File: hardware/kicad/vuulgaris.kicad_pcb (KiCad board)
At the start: 2 copper layers, 284.3 x 125 mm, 69 parts, among them J1 TFPUSH, J10 PJ-603_C41409498, J11 TYPE-C-31-M-12, J2 PJ-376, J3 PJ-376, J4 PJ-376, J5 PJ-376, J7 PJ-603_C41409498, J8 PJ-603_C41409498, J9 PJ-603_C41409498, SW4 CPG151101S03, SW5 CPG151101S03, SW6 CPG151101S03, SW7 CPG151101S03, U1 ES_DAISY_PATCH_SM_REV1, U3 MCP23017-E_SO, U4 MCP23017-E_SO, U5 AMS1117-3.3, U6 AMS1117-3.3, U7 DKM10E-12

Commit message: hardware: place the Daisy for the signals, and fix place.py's mirror flag
MIDI is dropped -- firmware goes on by opening the box -- so the micro-USB no
longer has to reach a wall and the Daisy's placement is unconstrained. It goes in
the dead band between the pot row and the electrodes, x[125.5,193.5] y[42.5,82.5].

Not beside the power stage. That is the intuitive answer and it is backwards:
weighting wire length by how much length actually hurts each signal, sitting on
the power stage scores 11875 against 5611. It does buy the shortest rails, 109mm
against 355mm, and that is worth almost nothing -- they are DC, so widen the
trace and the loss is millivolts. It pays for them with 244mm of extra analog
audio and 651mm of extra CV routed straight over the capacitive electrodes.

The scoring has a real hole worth knowing about: J2-J5 and J7-J10 are placed but
unwired, so netmap.json does not know where audio or CV terminate. The first run
silently returned empty AUDIO and CV columns and ranked the options on SPI and
power alone -- the two classes the argument does not rest on. Destinations are
supplied by hand for now; redo it once the jacks are wired.

Separately, place.py had `Lm` assigned in the pad-orientation loop and read again
in the overlap loop, where it held whatever footprint the earlier loop ended on.
Every box in the overlap and edge checks got the same arbitrary mirror flag. It
invented a 3.18mm RV3/RV4-vs-U1 collision, which is how it was noticed -- RV4's
local y is [-9.14,+4.4] and mirrored reads [-4.4,+9.14], moving its bottom edge
4.74mm. A check that fabricates a collision will hide one just as quietly. Third
mirror bug in this file.
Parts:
- moved U1 89.2 mm to (259.5, 112.5)
- moved J1 12.0 mm to (238.4, 142.1)
- turned J11 to 0 degrees
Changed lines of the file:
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@@
   )
   (footprint "vuulgaris:DAISY_PATCH_SM" (layer "F.Cu")
-    (at 180.0 153.0)
+    (at 259.5 112.5)
     (property "Sheetfile" "vuulgaris.kicad_sch")
     (property "Sheetname" "")
@@
   )
   (footprint "vuulgaris:USB-C_SMD-TYPE-C-31-M-12_1" (layer "B.Cu")
-    (at 379.2 54.0 -90)
+    (at 379.2 54.0)
     (property "Sheetfile" "vuulgaris.kicad_sch")
     (property "Sheetname" "")
     (property "ki_keywords" "USB Connectors")
     (attr smd)
-    (fp_text reference "J11" (at 0 6.474 90) (layer "B.SilkS")
+    (fp_text reference "J11" (at 0 6.474) (layer "B.SilkS")
         (effects (font (size 1 1) (thickness 0.15)) (justify mirror))
     )
-    (fp_text value "TYPE-C-31-M-12" (at 0 -6.474 90) (layer "B.Fab")
+    (fp_text value "TYPE-C-31-M-12" (at 0 -6.474) (layer "B.Fab")
         (effects (font (size 1 1) (thickness 0.15)) (justify mirror))
     )
-    (fp_text user "${REFERENCE}" (at 0 0 90) (layer "B.Fab")
+    (fp_text user "${REFERENCE}" (at 0 0) (layer "B.Fab")
         (effects (font (size 1 1) (thickness 0.15)) (justify mirror))
     )
@@
     (fp_line (start 4.47 2.26) (end 4.47 -5.09)
       (stroke (width 0.05) (type solid)) (layer "B.CrtYd"))
-    (pad "" thru_hole circle (at -2.9 1.21 270) (size 0.6 0.6) (drill 0.6) (layers "*.Cu" "*.Mask"))
-    (pad "" thru_hole circle (at 2.9 1.21 270) (size 0.6 0.6) (drill 0.6) (layers "*.Cu" "*.Mask"))
-    (pad "1" thru_hole oval (at 4.33 1.71 270) (size 1.2 2) (drill oval 0.799998 1.499997) (layers "*.Cu" "*.Mask")
+    (pad "" thru_hole circle (at -2.9 1.21) (size 0.6 0.6) (drill 0.6) (layers "*.Cu" "*.Mask"))
+    (pad "" thru_hole circle (at 2.9 1.21) (size 0.6 0.6) (drill 0.6) (layers "*.Cu" "*.Mask"))
+    (pad "1" thru_hole oval (at 4.33 1.71) (size 1.2 2) (drill oval 0.799998 1.499997) (layers "*.Cu" "*.Mask")
       (net 1 "/GND") (pinfunction "EH") (pintype "unspecified"))
-    (pad "2" thru_hole oval (at 4.33 -2.47 270) (size 1.2 1.8) (drill oval 0.799998 1.199998) (layers "*.Cu" "*.Mask")
+    (pad "2" thru_hole oval (at 4.33 -2.47) (size 1.2 1.8) (drill oval 0.799998 1.199998) (layers "*.Cu" "*.Mask")
       (net 1 "/GND") (pinfunction "EH") (pintype "unspecified"))
-    (pad "3" thru_hole oval (at -4.33 -2.47 270) (size 1.2 1.8) (drill oval 0.799998 1.199998) (layers "*.Cu" "*.Mask")
+    (pad "3" thru_hole oval (at -4.33 -2.47) (size 1.2 1.8) (drill oval 0.799998 1.199998) (layers "*.Cu" "*.Mask")
       (net 1 "/GND") (pinfunction "EH") (pintype "unspecified"))
-    (pad "4" thru_hole oval (at -4.33 1.71 270) (size 1.2 2) (drill oval 0.799998 1.499997) (layers "*.Cu" "*.Mask")
+    (pad "4" thru_hole oval (at -4.33 1.71) (size 1.2 2) (drill oval 0.799998 1.499997) (layers "*.Cu" "*.Mask")
       (net 1 "/GND") (pinfunction "EH") (pintype "unspecified"))
-    (pad "A1B12" smd custom (at -3.2 2.47 270) (size 0.005 0.005) (layers "B.Cu" "B.Paste" "B.Mask")
+    (pad "A1B12" smd custom (at -3.2 2.47) (size 0.005 0.005) (layers "B.Cu" "B.Paste" "B.Mask")
       (net 1 "/GND") (pinfunction "GND") (pintype "unspecified") (thermal_bridge_angle 90)
       (options (clearance outline) (anchor circle))
@@
           (width 0.1) (fill yes))
       ))
-    (pad "A4B9" smd custom (at -2.4 2.47 270) (size 0.005 0.005) (layers "B.Cu" "B.Paste" "B.Mask")
+    (pad "A4B9" smd custom (at -2.4 2.47) (size 0.005 0.005) (layers "B.Cu" "B.Paste" "B.Mask")
       (net 165 "/VBUS") (pinfunction "VBUS") (pintype "unspecified") (thermal_bridge_angle 90)
       (options (clearance outline) (anchor circle))
@@
           (width 0.1) (fill yes))
       ))
-    (pad "A5" smd rect (at -1.25 2.47 270) (size 0.3 1.3) (layers "B.Cu" "B.Paste" "B.Mask")
+    (pad "A5" smd rect (at -1.25 2.47) (size 0.3 1.3) (layers "B.Cu" "B.Paste" "B.Mask")
       (net 172 "/CC1") (pinfunction "CC1") (pintype "unspecified"))
-    (pad "A6" smd rect (at -0.25 2.47 270) (size 0.3 1.3) (layers "B.Cu" "B.Paste" "B.Mask")
+    (pad "A6" smd rect (at -0.25 2.47) (size 0.3 1.3) (layers "B.Cu" "B.Paste" "B.Mask")
       (net 174 "unconnected-(J11-DP1-PadA6)") (pinfunction "DP1") (pintype "unspecified+no_connect"))
-    (pad "A7" smd rect (at 0.25 2.47 270) (size 0.3 1.3) (layers "B.Cu" "B.Paste" "B.Mask")
+    (pad "A7" smd rect (at 0.25 2.47) (size 0.3 1.3) (layers "B.Cu" "B.Paste" "B.Mask")
       (net 175 "unconnected-(J11-DN1-PadA7)") (pinfunction "DN1") (pintype "unspecified+no_connect"))
-    (pad "A8" smd rect (at 1.25 2.47 270) (size 0.3 1.3) (layers "B.Cu" "B.Paste" "B.Mask")
+    (pad "A8" smd rect (at 1.25 2.47) (size 0.3 1.3) (layers "B.Cu" "B.Paste" "B.Mask")
       (net 177 "unconnected-(J11-SBU1-PadA8)") (pinfunction "SBU1") (pintype "unspecified+no_connect"))
-    (pad "B1A12" smd custom (at 3.2 2.47 270) (size 0.005 0.005) (layers "B.Cu" "B.Paste" "B.Mask")
+    (pad "B1A12" smd custom (at 3.2 2.47) (size 0.005 0.005) (layers "B.Cu" "B.Paste" "B.Mask")
       (net 1 "/GND") (pinfunction "GND") (pintype "unspecified") (thermal_bridge_angle 90)
       (options (clearance outline) (anchor circle))
@@
           (width 0.1) (fill yes))
       ))
-    (pad "B4A9" smd custom (at 2.4 2.47 270) (size 0.005 0.005) (layers "B.Cu" "B.Paste" "B.Mask")
+    (pad "B4A9" smd custom (at 2.4 2.47) (size 0.005 0.005) (layers "B.Cu" "B.Paste" "B.Mask")
       (net 165 "/VBUS") (pinfunction "VBUS") (pintype "unspecified") (thermal_bridge_angle 90)
       (options (clearance outline) (anchor circle))
@@
           (width 0.1) (fill yes))
       ))
-    (pad "B5" smd rect (at 1.75 2.47 270) (size 0.3 1.3) (layers "B.Cu" "B.Paste" "B.Mask")
+    (pad "B5" smd rect (at 1.75 2.47) (size 0.3 1.3) (layers "B.Cu" "B.Paste" "B.Mask")
       (net 178 "/CC2") (pinfunction "CC2") (pintype "unspecified"))
-    (pad "B6" smd rect (at 0.75 2.47 270) (size 0.3 1.3) (layers "B.Cu" "B.Paste" "B.Mask")
+    (pad "B6" smd rect (at 0.75 2.47) (size 0.3 1.3) (layers "B.Cu" "B.Paste" "B.Mask")
       (net 176 "unconnected-(J11-DP2-PadB6)") (pinfunction "DP2") (pintype "unspecified+no_connect"))
-    (pad "B7" smd rect (at -0.75 2.47 270) (size 0.3 1.3) (layers "B.Cu" "B.Paste" "B.Mask")
+    (pad "B7" smd rect (at -0.75 2.47) (size 0.3 1.3) (layers "B.Cu" "B.Paste" "B.Mask")
       (net 173 "unconnected-(J11-DN2-PadB7)") (pinfunction "DN2") (pintype "unspecified+no_connect"))
-    (pad "B8" smd rect (at -1.75 2.47 270) (size 0.3 1.3) (layers "B.Cu" "B.Paste" "B.Mask")
+    (pad "B8" smd rect (at -1.75 2.47) (size 0.3 1.3) (layers "B.Cu" "B.Paste" "B.Mask")
       (net 171 "unconnected-(J11-SBU2-PadB8)") (pinfunction "SBU2") (pintype "unspecified+no_connect"))
     (model "lib/vuulgaris.3dshapes/USB-C_SMD-TYPE-C-31-M-12_1.wrl"
@@
   )
   (footprint "vuulgaris:TF-SMD_TF-PUSH" (layer "B.Cu")
-    (at 226.5 143.4 180)
+    (at 238.4 142.1 180)
     (property "Sheetfile" "vuulgaris.kicad_sch")
     (property "Sheetname" "")

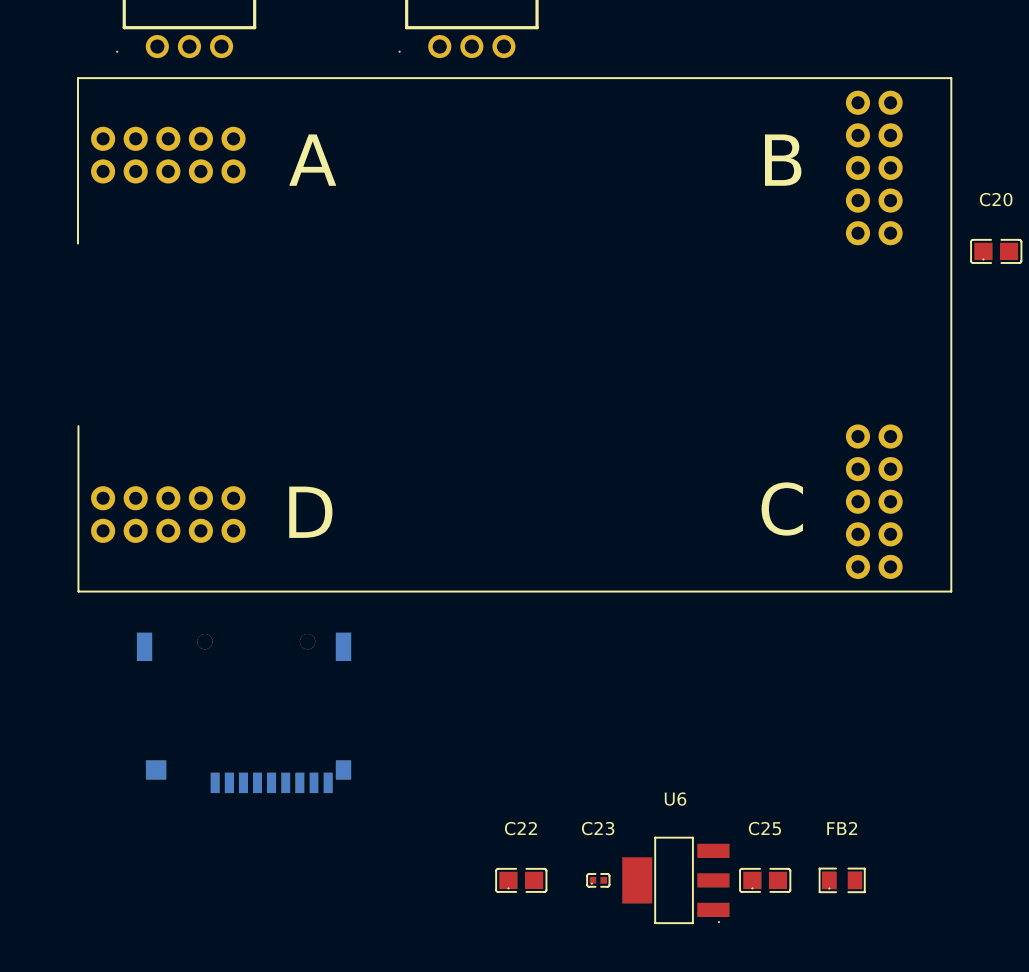
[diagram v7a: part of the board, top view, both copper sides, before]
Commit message: hardware: flip the Daisy to the back, move the SD clear of it
U1 goes to B.Cu. On the front it was competing for the gap between the main PCB
and the faceplate, directly under the electrodes, which is the worst place for
it. Position is unchanged at x[125.5,193.5] y[42.5,82.5] -- the carrier's pad set
is symmetric in Y, so mirroring does not move its outline.

J1 moves to x[129.7,146.4] y[93.9,109.7]. The slot mouth is local +y, so the card
ejects toward the bottom edge; with U1 now on the same face the socket needs
clearance in front of the mouth rather than merely no overlap. It gets 15.3mm to
the board edge and 11.4mm back to the Daisy.

Flagging an open bug found while verifying this, in design-state. J7 and J1 are
both on B.Cu but store their local pad coordinates differently -- J7 with local Y
negated, J1 identical to the library. KiCad negates local Y when it flips a
footprint, so J1 appears never to have been flipped, only relabelled, which would
mirror the SD contacts and put SD_CMD/CLK/D0 on the wrong physical pins. Nothing
in ERC or DRC can see that: the netlist stays self-consistent, the pads are just
not where the part's contacts are. Needs checking in Pcbnew, not by more
arithmetic.

Also worth recording: the obvious Gerber check for U1's flip is worthless. Its
A and D headers are mirror images of each other, so the mirrored and unmirrored
hypotheses produce identical pad SETS and both score 0.000mm against the plotted
flashes. A test that cannot fail is not a test.
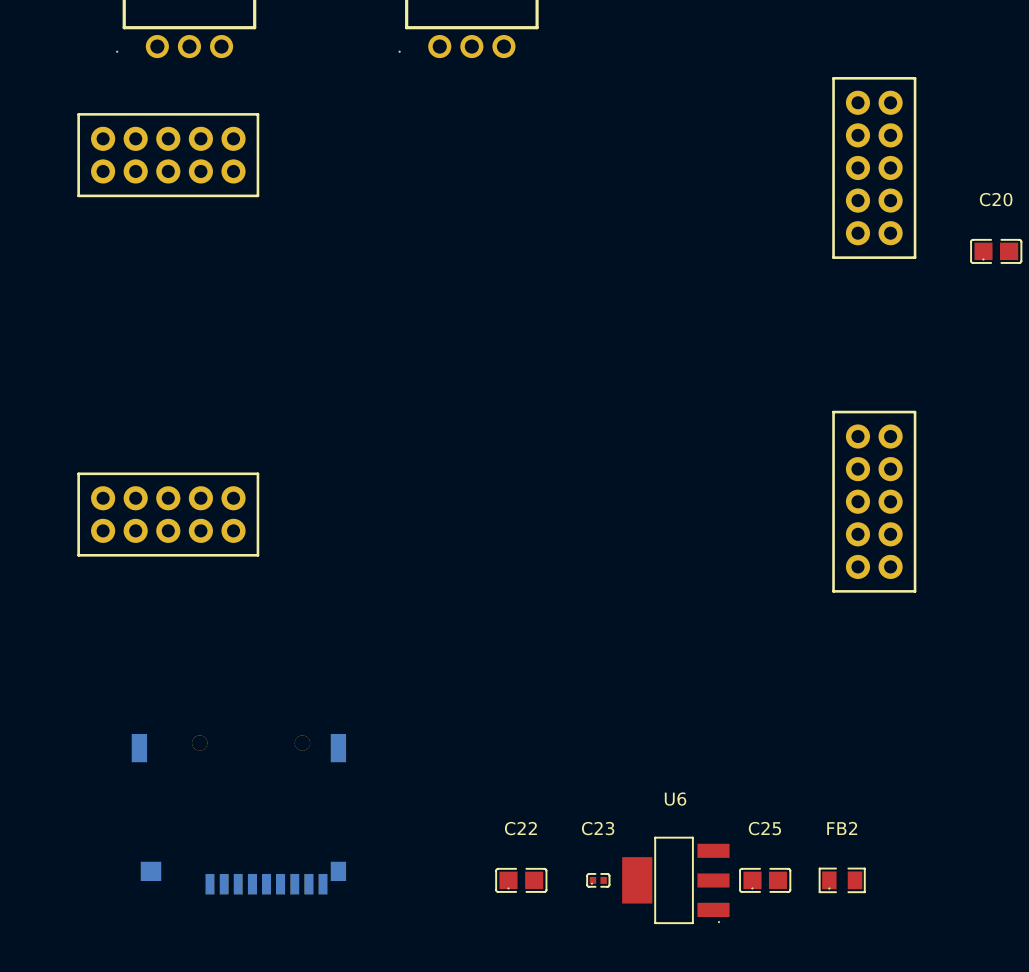
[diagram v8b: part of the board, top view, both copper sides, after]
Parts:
- U1: moved to B.Cu
- moved J1 7.91 mm to (238.0, 150.0)
